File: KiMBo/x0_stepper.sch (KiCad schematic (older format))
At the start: 25 parts, among them U20 TMC2130

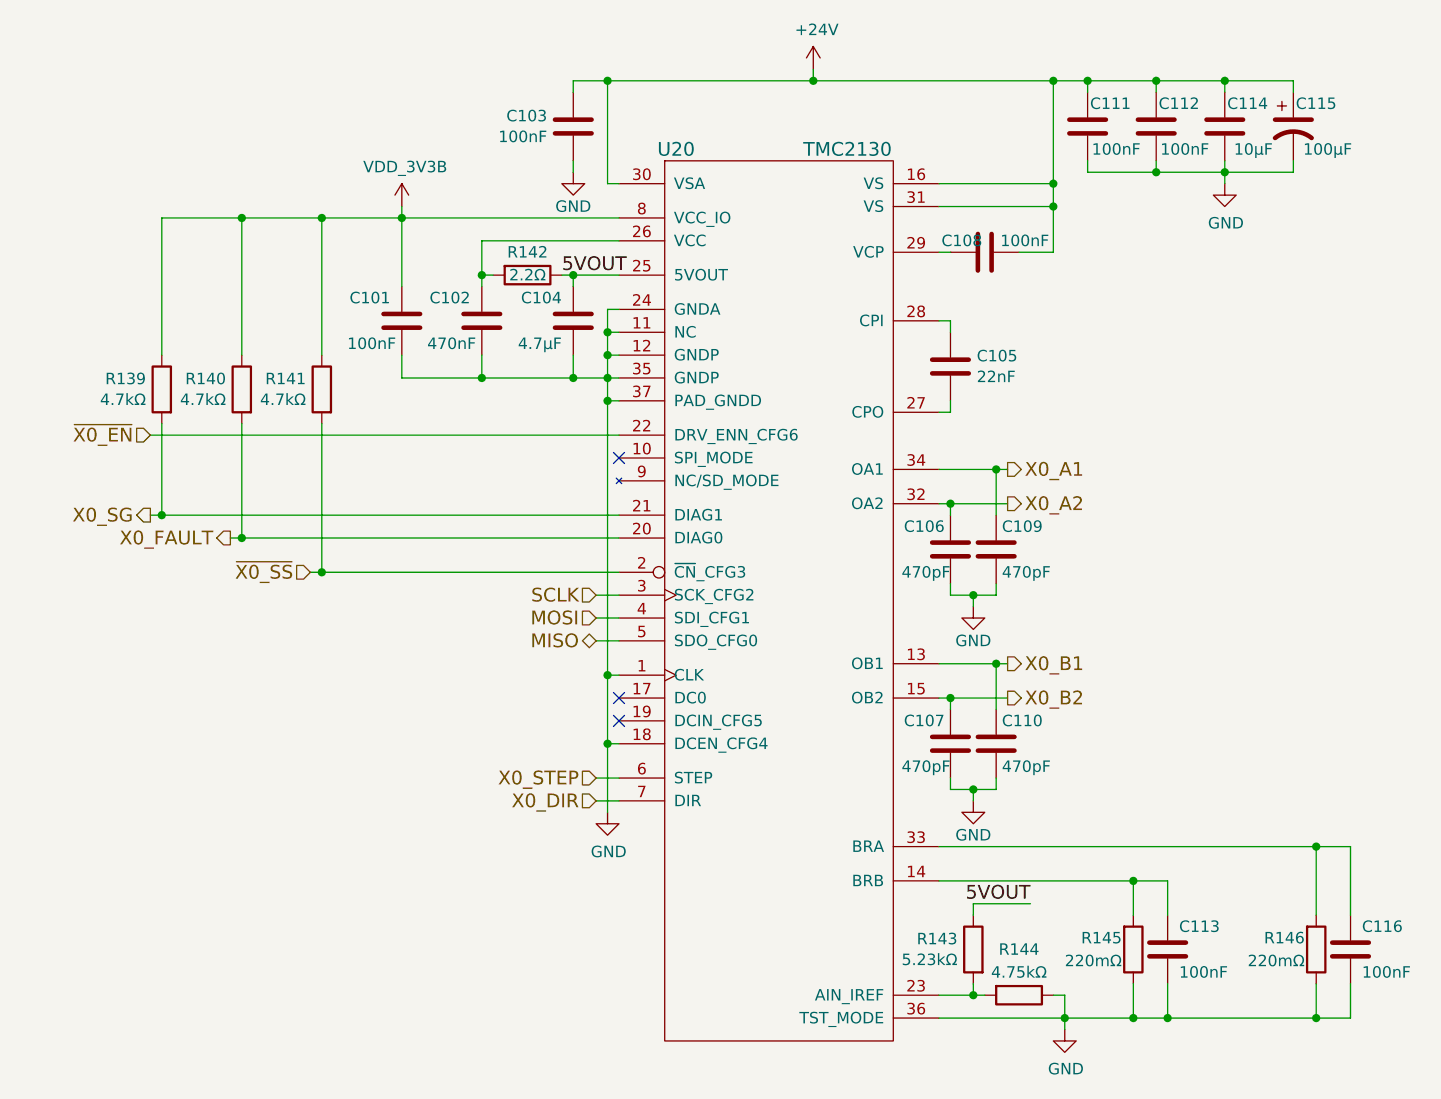
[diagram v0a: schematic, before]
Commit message: Leave SPI0 free for a display, reassign pins so SPI1 is available
Fix some typos/errors
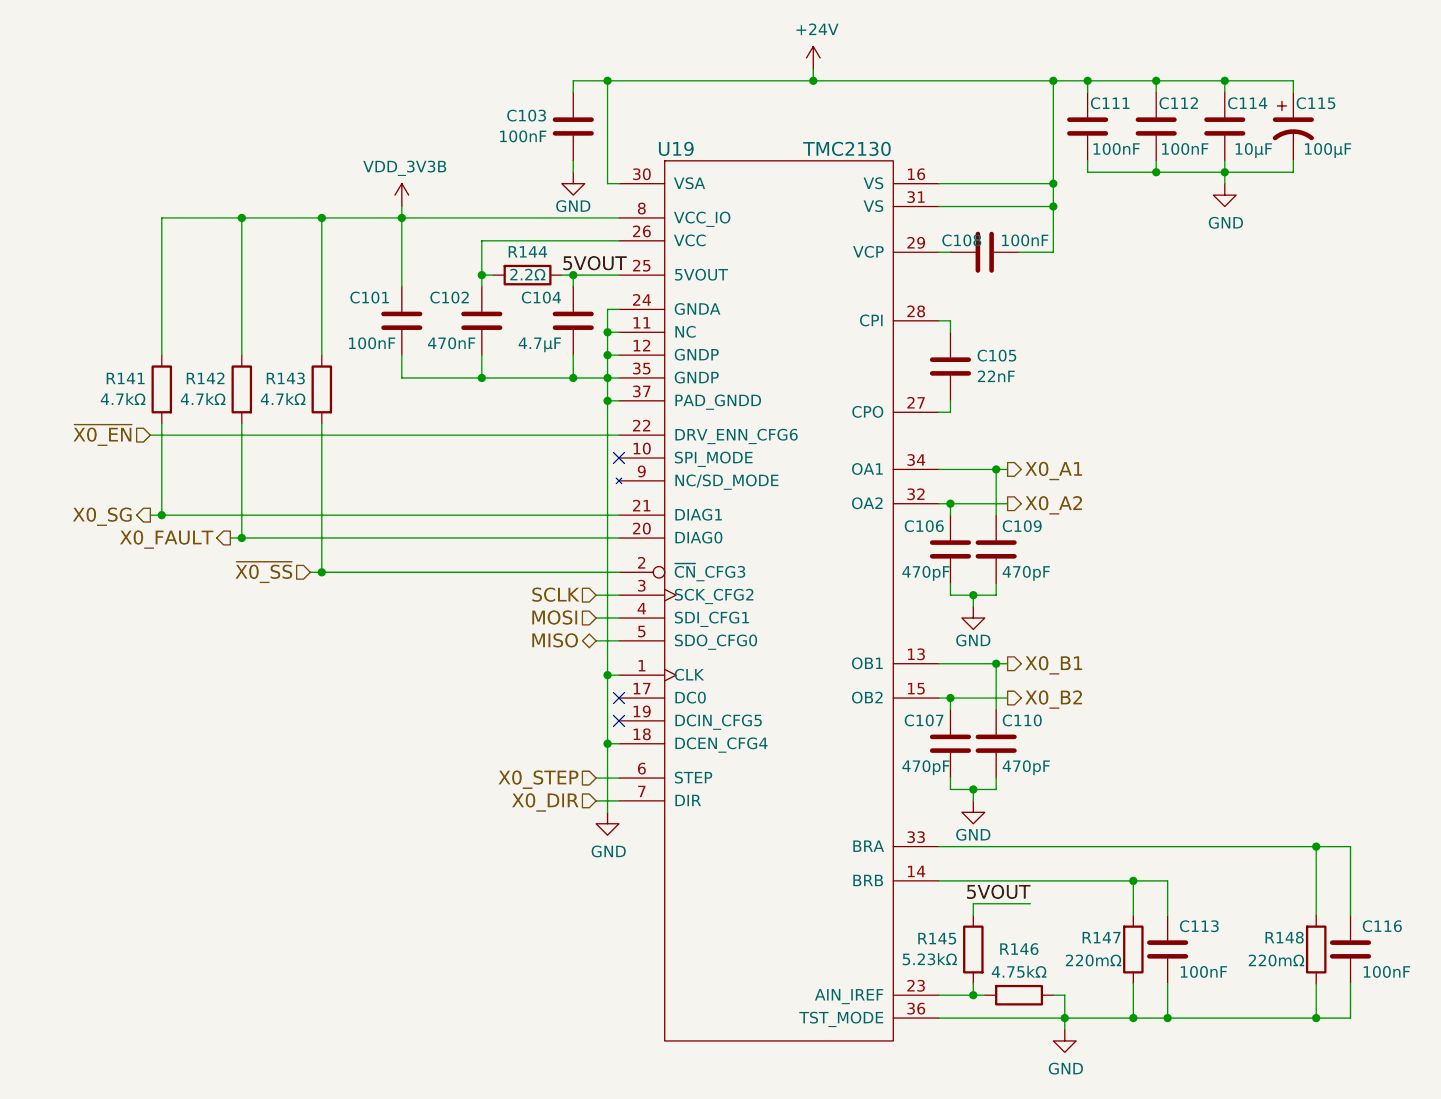
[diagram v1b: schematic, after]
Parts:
- renumbered R139 to R141, R140 to R142, R141 to R143, R142 to R144, R143 to R145, R144 to R146, R145 to R147, R146 to R148, U20 to U19
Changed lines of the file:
@@
 $EndComp
 $Comp
-L GND #PWR0208
+L GND #PWR0207
 U 1 1 58C092D2
 P 7500 3300
-F 0 "#PWR0208" H 7500 3050 50  0001 C CNN
+F 0 "#PWR0207" H 7500 3050 50  0001 C CNN
 F 1 "GND" H 7500 3150 50  0000 C CNN
 F 2 "" H 7500 3300 50  0000 C CNN
@@
 $EndComp
 $Comp
-L GND #PWR0209
+L GND #PWR0208
 U 1 1 5BA7E141
 P 10350 3350
-F 0 "#PWR0209" H 10350 3100 50  0001 C CNN
+F 0 "#PWR0208" H 10350 3100 50  0001 C CNN
 F 1 "GND" H 10355 3177 50  0000 C CNN
 F 2 "" H 10350 3350 50  0000 C CNN
@@
 $EndComp
 $Comp
-L +24V #PWR0210
+L +24V #PWR0209
 U 1 1 58C092E5
 P 8550 2850
-F 0 "#PWR0210" H 8550 2700 50  0001 C CNN
+F 0 "#PWR0209" H 8550 2700 50  0001 C CNN
 F 1 "+24V" H 8565 3023 50  0000 C CNN
 F 2 "" H 8550 2850 50  0000 C CNN
@@
 $EndComp
 $Comp
-L R R146
+L R R148
 U 1 1 58C092F2
 P 10750 6700
-F 0 "R146" H 10700 6650 50  0000 R CNN
+F 0 "R148" H 10700 6650 50  0000 R CNN
 F 1 "220mΩ" H 10700 6750 50  0000 R CNN
 F 2 "" V 10680 6700 50  0001 C CNN
@@
 $EndComp
 $Comp
-L R R145
+L R R147
 U 1 1 58C092F9
 P 9950 6700
-F 0 "R145" H 9900 6650 50  0000 R CNN
+F 0 "R147" H 9900 6650 50  0000 R CNN
 F 1 "220mΩ" H 9900 6750 50  0000 R CNN
 F 2 "" V 9880 6700 50  0001 C CNN
@@
 $EndComp
 $Comp
-L GND #PWR0211
+L GND #PWR0210
 U 1 1 5BA7E146
 P 9650 7050
-F 0 "#PWR0211" H 9650 6800 50  0001 C CNN
+F 0 "#PWR0210" H 9650 6800 50  0001 C CNN
 F 1 "GND" H 9655 6877 50  0000 C CNN
 F 2 "" H 9650 7050 50  0000 C CNN
@@
 NoConn ~ 7700 5600
 $Comp
-L R R142
+L R R144
 U 1 1 5BA7E147
 P 7300 3750
-F 0 "R142" V 7200 3750 50  0000 C CNN
+F 0 "R144" V 7200 3750 50  0000 C CNN
 F 1 "2.2Ω" V 7300 3750 50  0000 C CNN
 F 2 "" V 7230 3750 50  0001 C CNN
@@
 NoConn ~ 7700 5700
 $Comp
-L GND #PWR0212
+L GND #PWR0211
 U 1 1 5BA7E149
 P 7650 6100
-F 0 "#PWR0212" H 7650 5850 50  0001 C CNN
+F 0 "#PWR0211" H 7650 5850 50  0001 C CNN
 F 1 "GND" H 7655 5927 50  0000 C CNN
 F 2 "" H 7650 6100 50  0000 C CNN
@@
 X0_FAULT
 $Comp
-L R R140
+L R R142
 U 1 1 58C09331
 P 6050 4250
-F 0 "R140" H 6119 4296 50  0000 L CNN
+F 0 "R142" H 6119 4296 50  0000 L CNN
 F 1 "4.7kΩ" H 6119 4205 50  0000 L CNN
 F 2 "" V 5980 4250 50  0001 C CNN
@@
 5VOUT
 $Comp
-L R R143
+L R R145
 U 1 1 5BA7E14D
 P 9250 6700
-F 0 "R143" H 9319 6746 50  0000 L CNN
+F 0 "R145" H 9319 6746 50  0000 L CNN
 F 1 "5.23kΩ" H 9319 6655 50  0000 L CNN
 F 2 "" V 9180 6700 50  0001 C CNN
@@
 5VOUT
 $Comp
-L R R144
+L R R146
 U 1 1 5BA7E14E
 P 9450 6900
-F 0 "R144" V 9250 6900 50  0000 C CNN
+F 0 "R146" V 9250 6900 50  0000 C CNN
 F 1 "4.75kΩ" V 9350 6900 50  0000 C CNN
 F 2 "" V 9380 6900 50  0001 C CNN
@@
 $EndComp
 $Comp
-L R R141
+L R R143
 U 1 1 58C09353
 P 6400 4250
-F 0 "R141" H 6469 4296 50  0000 L CNN
+F 0 "R143" H 6469 4296 50  0000 L CNN
 F 1 "4.7kΩ" H 6469 4205 50  0000 L CNN
 F 2 "" V 6330 4250 50  0001 C CNN
@@
 $EndComp
 $Comp
-L GND #PWR0213
+L GND #PWR0212
 U 1 1 58C0936A
 P 9250 5200
-F 0 "#PWR0213" H 9250 4950 50  0001 C CNN
+F 0 "#PWR0212" H 9250 4950 50  0001 C CNN
 F 1 "GND" H 9250 5050 50  0000 C CNN
 F 2 "" H 9250 5200 50  0000 C CNN
@@
 $EndComp
 $Comp
-L GND #PWR0214
+L GND #PWR0213
 U 1 1 58C0937E
 P 9250 6050
-F 0 "#PWR0214" H 9250 5800 50  0001 C CNN
+F 0 "#PWR0213" H 9250 5800 50  0001 C CNN
 F 1 "GND" H 9250 5900 50  0000 C CNN
 F 2 "" H 9250 6050 50  0000 C CNN
@@
 $EndComp
 $Comp
-L TMC2130 U20
+L TMC2130 U19
 U 1 1 58C0938B
 P 8400 4700
-F 0 "U20" H 7950 6200 60  0000 C CNN
+F 0 "U19" H 7950 6200 60  0000 C CNN
 F 1 "TMC2130" H 8700 6200 60  0000 C CNN
 F 2 "" H 8400 5000 60  0001 C CNN
@@
 	9150 6000 9150 5950
 $Comp
-L R R139
+L R R141
 U 1 1 5BA7E158
 P 5700 4250
-F 0 "R139" H 5769 4296 50  0000 L CNN
+F 0 "R141" H 5769 4296 50  0000 L CNN
 F 1 "4.7kΩ" H 5769 4205 50  0000 L CNN
 F 2 "" V 5630 4250 50  0001 C CNN
@@
 	5700 3500 7700 3500
 $Comp
-L VDD_3V3B #PWR0215
+L VDD_3V3B #PWR0214
 U 1 1 5A2FF856
 P 6750 3450
-F 0 "#PWR0215" H 6750 3300 50  0001 C CNN
+F 0 "#PWR0214" H 6750 3300 50  0001 C CNN
 F 1 "VDD_3V3B" H 6765 3623 50  0000 C CNN
 F 2 "" H 6750 3450 50  0000 C CNN

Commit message: Use fixed 5V LM2592HV Buck, include SPI0 header for LCD
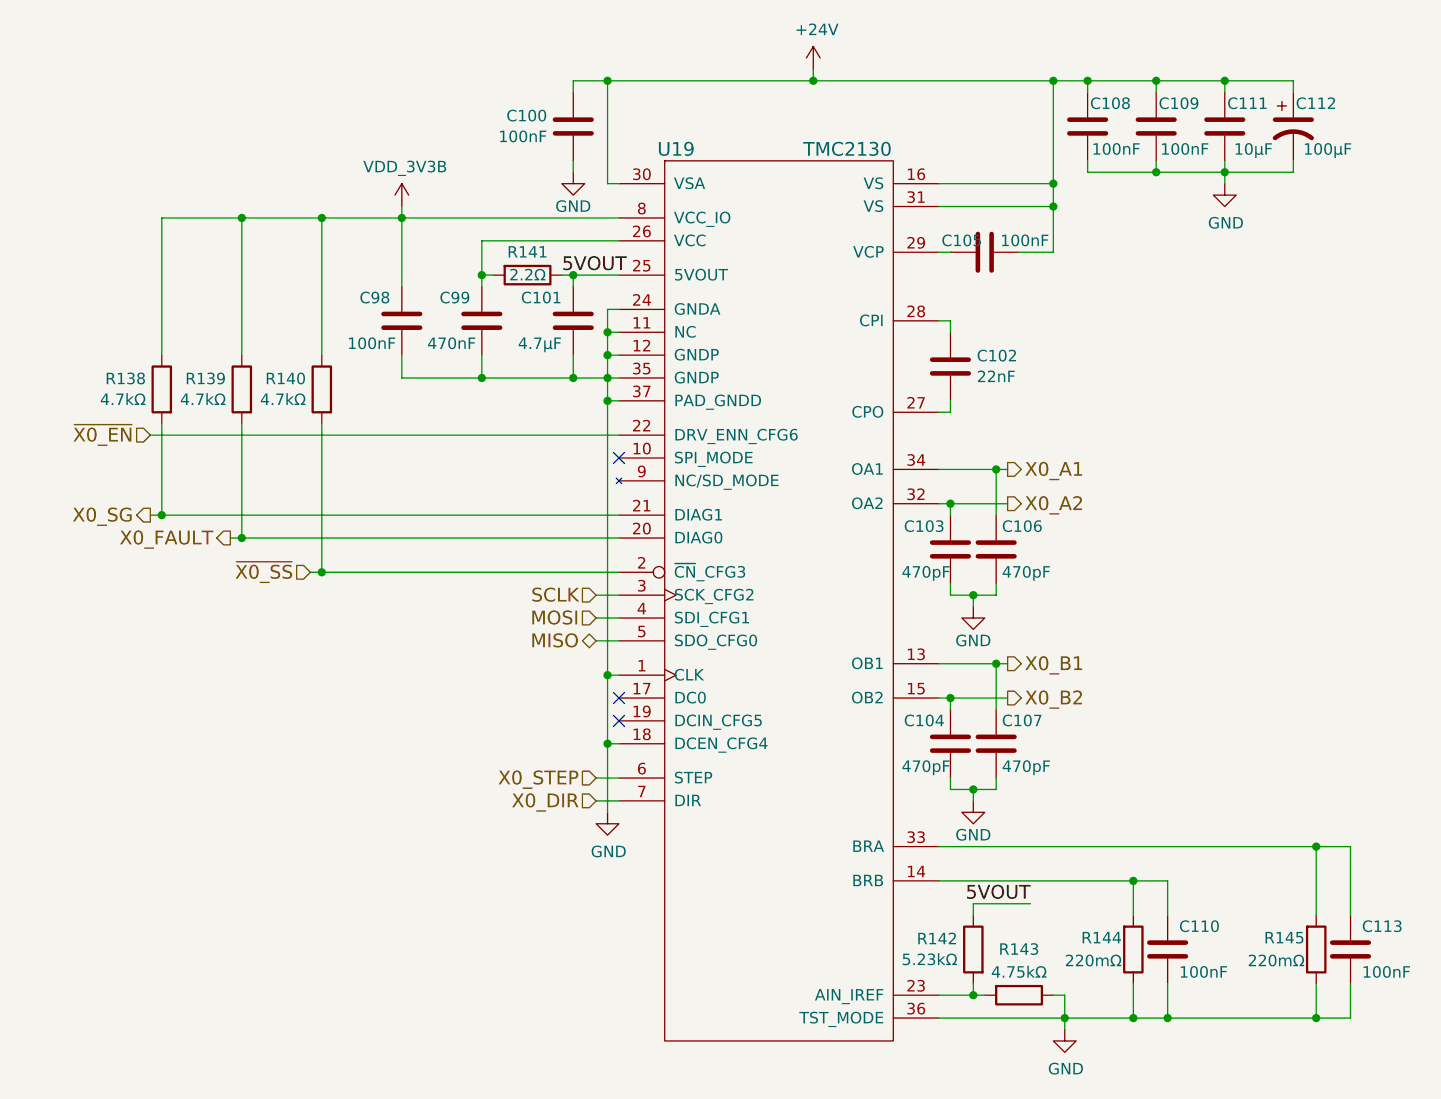
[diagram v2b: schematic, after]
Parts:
- renumbered C103 to C100, C104 to C101, C105 to C102, C106 to C103, C107 to C104, C108 to C105, C109 to C106, C110 to C107, C111 to C108, C112 to C109, C113 to C110, C114 to C111, C115 to C112, C116 to C113, C101 to C98, C102 to C99, R141 to R138, R142 to R139, R143 to R140, R144 to R141, R145 to R142, R146 to R143, R147 to R144, R148 to R145
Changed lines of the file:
@@
 X0_SG
 $Comp
-L C C103
+L C C100
 U 1 1 5BA7E13B
 P 7500 3100
-F 0 "C103" H 7386 3054 50  0000 R CNN
+F 0 "C100" H 7386 3054 50  0000 R CNN
 F 1 "100nF" H 7386 3145 50  0000 R CNN
 F 2 "Capacitors_SMD:C_0603" H 7538 2950 50  0001 C CNN
@@
 $EndComp
 $Comp
-L C C108
+L C C105
 U 1 1 5BA7E13C
 P 9300 3650
-F 0 "C108" V 9250 3550 50  0000 C CNN
+F 0 "C105" V 9250 3550 50  0000 C CNN
 F 1 "100nF" V 9250 3825 50  0000 C CNN
 F 2 "Capacitors_SMD:C_0603" H 9338 3500 50  0001 C CNN
@@
 $EndComp
 $Comp
-L CP1 C115
+L CP1 C112
 U 1 1 58C092C4
 P 10650 3100
-F 0 "C115" H 10750 3200 50  0000 C CNN
+F 0 "C112" H 10750 3200 50  0000 C CNN
 F 1 "100μF" H 10800 3000 50  0000 C CNN
 F 2 "Capacitors_SMD:c_elec_8x10" H 10650 3100 50  0001 C CNN
@@
 $EndComp
 $Comp
-L C C111
+L C C108
 U 1 1 58C092CB
 P 9750 3100
-F 0 "C111" H 9650 3200 50  0000 C CNN
+F 0 "C108" H 9650 3200 50  0000 C CNN
 F 1 "100nF" H 9625 3000 50  0000 C CNN
 F 2 "Capacitors_SMD:C_0603" H 9788 2950 50  0001 C CNN
@@
 $EndComp
 $Comp
-L GND #PWR0207
+L GND #PWR0202
 U 1 1 58C092D2
 P 7500 3300
-F 0 "#PWR0207" H 7500 3050 50  0001 C CNN
+F 0 "#PWR0202" H 7500 3050 50  0001 C CNN
 F 1 "GND" H 7500 3150 50  0000 C CNN
 F 2 "" H 7500 3300 50  0000 C CNN
@@
 $EndComp
 $Comp
-L C C112
+L C C109
 U 1 1 5BA7E140
 P 10050 3100
-F 0 "C112" H 9950 3200 50  0000 C CNN
+F 0 "C109" H 9950 3200 50  0000 C CNN
 F 1 "100nF" H 9925 3000 50  0000 C CNN
 F 2 "Capacitors_SMD:C_0603" H 10088 2950 50  0001 C CNN
@@
 $EndComp
 $Comp
-L GND #PWR0208
+L GND #PWR0203
 U 1 1 5BA7E141
 P 10350 3350
-F 0 "#PWR0208" H 10350 3100 50  0001 C CNN
+F 0 "#PWR0203" H 10350 3100 50  0001 C CNN
 F 1 "GND" H 10355 3177 50  0000 C CNN
 F 2 "" H 10350 3350 50  0000 C CNN
@@
 $EndComp
 $Comp
-L +24V #PWR0209
+L +24V #PWR0204
 U 1 1 58C092E5
 P 8550 2850
-F 0 "#PWR0209" H 8550 2700 50  0001 C CNN
+F 0 "#PWR0204" H 8550 2700 50  0001 C CNN
 F 1 "+24V" H 8565 3023 50  0000 C CNN
 F 2 "" H 8550 2850 50  0000 C CNN
@@
 $EndComp
 $Comp
-L C C105
+L C C102
 U 1 1 58C092EB
 P 9150 4150
-F 0 "C105" H 9265 4196 50  0000 L CNN
+F 0 "C102" H 9265 4196 50  0000 L CNN
 F 1 "22nF" H 9265 4105 50  0000 L CNN
 F 2 "Capacitors_SMD:C_0402" H 9188 4000 50  0001 C CNN
@@
 $EndComp
 $Comp
-L R R148
+L R R145
 U 1 1 58C092F2
 P 10750 6700
-F 0 "R148" H 10700 6650 50  0000 R CNN
+F 0 "R145" H 10700 6650 50  0000 R CNN
 F 1 "220mΩ" H 10700 6750 50  0000 R CNN
 F 2 "" V 10680 6700 50  0001 C CNN
@@
 $EndComp
 $Comp
-L R R147
+L R R144
 U 1 1 58C092F9
 P 9950 6700
-F 0 "R147" H 9900 6650 50  0000 R CNN
+F 0 "R144" H 9900 6650 50  0000 R CNN
 F 1 "220mΩ" H 9900 6750 50  0000 R CNN
 F 2 "" V 9880 6700 50  0001 C CNN
@@
 $EndComp
 $Comp
-L GND #PWR0210
+L GND #PWR0205
 U 1 1 5BA7E146
 P 9650 7050
-F 0 "#PWR0210" H 9650 6800 50  0001 C CNN
+F 0 "#PWR0205" H 9650 6800 50  0001 C CNN
 F 1 "GND" H 9655 6877 50  0000 C CNN
 F 2 "" H 9650 7050 50  0000 C CNN
@@
 NoConn ~ 7700 5600
 $Comp
-L R R144
+L R R141
 U 1 1 5BA7E147
 P 7300 3750
-F 0 "R144" V 7200 3750 50  0000 C CNN
+F 0 "R141" V 7200 3750 50  0000 C CNN
 F 1 "2.2Ω" V 7300 3750 50  0000 C CNN
 F 2 "" V 7230 3750 50  0001 C CNN
@@
 $EndComp
 $Comp
-L C C102
+L C C99
 U 1 1 5BA7E148
 P 7100 3950
-F 0 "C102" H 7150 4050 50  0000 L CNN
+F 0 "C99" H 7150 4050 50  0000 L CNN
 F 1 "470nF" H 7125 3850 50  0000 L CNN
 F 2 "Capacitors_SMD:C_0603" H 7138 3800 50  0001 C CNN
@@
 NoConn ~ 7700 5700
 $Comp
-L GND #PWR0211
+L GND #PWR0206
 U 1 1 5BA7E149
 P 7650 6100
-F 0 "#PWR0211" H 7650 5850 50  0001 C CNN
+F 0 "#PWR0206" H 7650 5850 50  0001 C CNN
 F 1 "GND" H 7655 5927 50  0000 C CNN
 F 2 "" H 7650 6100 50  0000 C CNN
@@
 $EndComp
 $Comp
-L C C113
+L C C110
 U 1 1 5BA7E14A
 P 10100 6700
-F 0 "C113" H 10150 6800 50  0000 L CNN
+F 0 "C110" H 10150 6800 50  0000 L CNN
 F 1 "100nF" H 10150 6600 50  0000 L CNN
 F 2 "Capacitors_SMD:C_0603" H 10138 6550 50  0001 C CNN
@@
 X0_FAULT
 $Comp
-L R R142
+L R R139
 U 1 1 58C09331
 P 6050 4250
-F 0 "R142" H 6119 4296 50  0000 L CNN
+F 0 "R139" H 6119 4296 50  0000 L CNN
 F 1 "4.7kΩ" H 6119 4205 50  0000 L CNN
 F 2 "" V 5980 4250 50  0001 C CNN
@@
 NoConn ~ 7700 4550
 $Comp
-L C C104
+L C C101
 U 1 1 5BA7E14C
 P 7500 3950
-F 0 "C104" H 7550 4050 50  0000 L CNN
+F 0 "C101" H 7550 4050 50  0000 L CNN
 F 1 "4.7μF" H 7550 3850 50  0000 L CNN
 F 2 "Capacitors_SMD:C_0402" H 7538 3800 50  0001 C CNN
@@
 5VOUT
 $Comp
-L R R145
+L R R142
 U 1 1 5BA7E14D
 P 9250 6700
-F 0 "R145" H 9319 6746 50  0000 L CNN
+F 0 "R142" H 9319 6746 50  0000 L CNN
 F 1 "5.23kΩ" H 9319 6655 50  0000 L CNN
 F 2 "" V 9180 6700 50  0001 C CNN
@@
 5VOUT
 $Comp
-L R R146
+L R R143
 U 1 1 5BA7E14E
 P 9450 6900
-F 0 "R146" V 9250 6900 50  0000 C CNN
+F 0 "R143" V 9250 6900 50  0000 C CNN
 F 1 "4.75kΩ" V 9350 6900 50  0000 C CNN
 F 2 "" V 9380 6900 50  0001 C CNN
@@
 $EndComp
 $Comp
-L R R143
+L R R140
 U 1 1 58C09353
 P 6400 4250
-F 0 "R143" H 6469 4296 50  0000 L CNN
+F 0 "R140" H 6469 4296 50  0000 L CNN
 F 1 "4.7kΩ" H 6469 4205 50  0000 L CNN
 F 2 "" V 6330 4250 50  0001 C CNN
@@
 $EndComp
 $Comp
-L C C116
+L C C113
 U 1 1 58C0935A
 P 10900 6700
-F 0 "C116" H 10950 6800 50  0000 L CNN
+F 0 "C113" H 10950 6800 50  0000 L CNN
 F 1 "100nF" H 10950 6600 50  0000 L CNN
 F 2 "Capacitors_SMD:C_0603" H 10938 6550 50  0001 C CNN
@@
 $EndComp
 $Comp
-L C C106
+L C C103
 U 1 1 58C09363
 P 9150 4950
-F 0 "C106" H 9175 5050 50  0000 L CNN
+F 0 "C103" H 9175 5050 50  0000 L CNN
 F 1 "470pF" H 9150 4850 50  0000 L CNN
 F 2 "Capacitors_SMD:C_0603" H 9188 4800 50  0001 C CNN
@@
 $EndComp
 $Comp
-L GND #PWR0212
+L GND #PWR0207
 U 1 1 58C0936A
 P 9250 5200
-F 0 "#PWR0212" H 9250 4950 50  0001 C CNN
+F 0 "#PWR0207" H 9250 4950 50  0001 C CNN
 F 1 "GND" H 9250 5050 50  0000 C CNN
 F 2 "" H 9250 5200 50  0000 C CNN
@@
 $EndComp
 $Comp
-L C C109
+L C C106
 U 1 1 58C09370
 P 9350 4950
-F 0 "C109" H 9375 5050 50  0000 L CNN
+F 0 "C106" H 9375 5050 50  0000 L CNN
 F 1 "470pF" H 9375 4850 50  0000 L CNN
 F 2 "Capacitors_SMD:C_0603" H 9388 4800 50  0001 C CNN
@@
 $EndComp
 $Comp
-L C C107
+L C C104
 U 1 1 5BA7E154
 P 9150 5800
-F 0 "C107" H 9175 5900 50  0000 L CNN
+F 0 "C104" H 9175 5900 50  0000 L CNN
 F 1 "470pF" H 9150 5700 50  0000 L CNN
 F 2 "Capacitors_SMD:C_0603" H 9188 5650 50  0001 C CNN
@@
 $EndComp
 $Comp
-L GND #PWR0213
+L GND #PWR0208
 U 1 1 58C0937E
 P 9250 6050
-F 0 "#PWR0213" H 9250 5800 50  0001 C CNN
+F 0 "#PWR0208" H 9250 5800 50  0001 C CNN
 F 1 "GND" H 9250 5900 50  0000 C CNN
 F 2 "" H 9250 6050 50  0000 C CNN
@@
 $EndComp
 $Comp
-L C C110
+L C C107
 U 1 1 58C09384
 P 9350 5800
-F 0 "C110" H 9375 5900 50  0000 L CNN
+F 0 "C107" H 9375 5900 50  0000 L CNN
 F 1 "470pF" H 9375 5700 50  0000 L CNN
 F 2 "Capacitors_SMD:C_0603" H 9388 5650 50  0001 C CNN
@@
 	9150 6000 9150 5950
 $Comp
-L R R141
+L R R138
 U 1 1 5BA7E158
 P 5700 4250
-F 0 "R141" H 5769 4296 50  0000 L CNN
+F 0 "R138" H 5769 4296 50  0000 L CNN
 F 1 "4.7kΩ" H 5769 4205 50  0000 L CNN
 F 2 "" V 5630 4250 50  0001 C CNN
@@
 Connection ~ 6050 3500
 $Comp
-L C C114
+L C C111
 U 1 1 5BA7E159
 P 10350 3100
-F 0 "C114" H 10250 3200 50  0000 C CNN
+F 0 "C111" H 10250 3200 50  0000 C CNN
 F 1 "10μF" H 10225 3000 50  0000 C CNN
 F 2 "Capacitors_SMD:C_0805" H 10388 2950 50  0001 C CNN
@@
 	5700 3500 7700 3500
 $Comp
-L VDD_3V3B #PWR0214
+L VDD_3V3B #PWR0209
 U 1 1 5A2FF856
 P 6750 3450
-F 0 "#PWR0214" H 6750 3300 50  0001 C CNN
+F 0 "#PWR0209" H 6750 3300 50  0001 C CNN
 F 1 "VDD_3V3B" H 6765 3623 50  0000 C CNN
 F 2 "" H 6750 3450 50  0000 C CNN
@@
 $EndComp
 $Comp
-L C C101
+L C C98
 U 1 1 5A89853C
 P 6750 3950
-F 0 "C101" H 6800 4050 50  0000 L CNN
+F 0 "C98" H 6800 4050 50  0000 L CNN
 F 1 "100nF" H 6775 3850 50  0000 L CNN
 F 2 "Capacitors_SMD:C_0603" H 6788 3800 50  0001 C CNN
